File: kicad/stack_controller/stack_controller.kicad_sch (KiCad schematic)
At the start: 47 parts

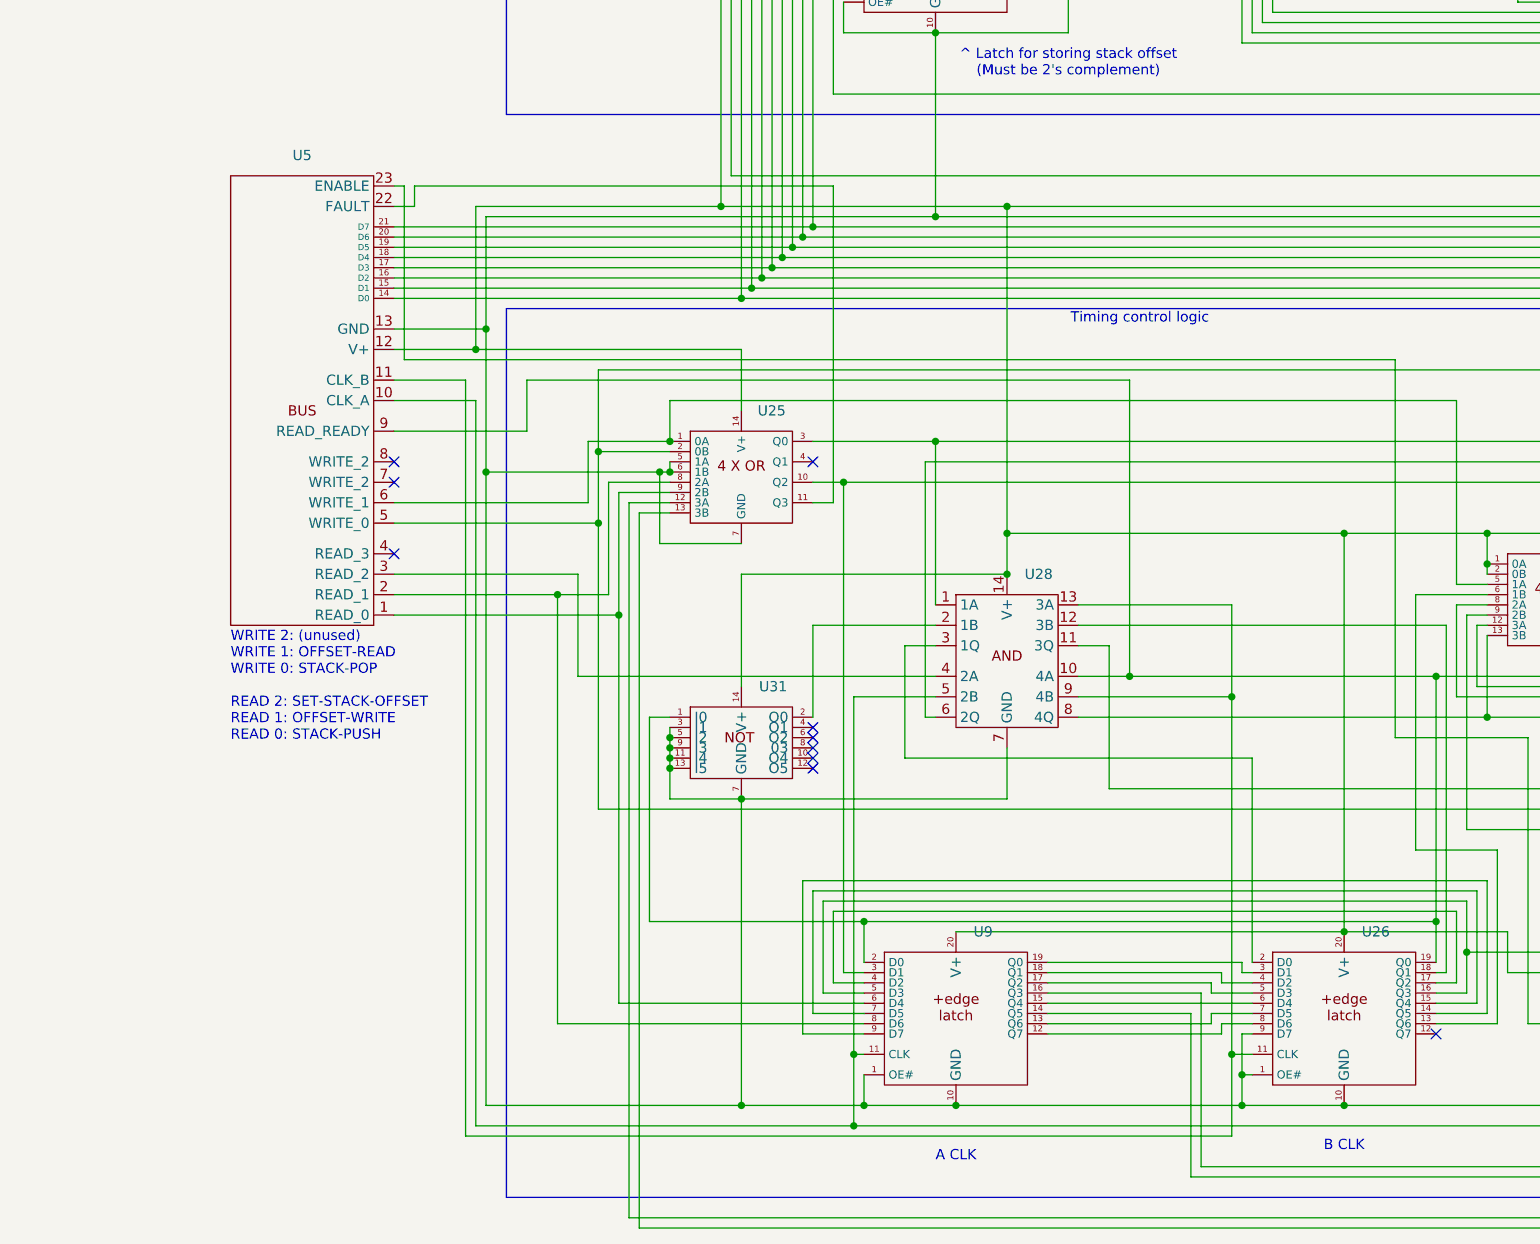
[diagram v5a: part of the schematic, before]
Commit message: Increased clock PCB clearances
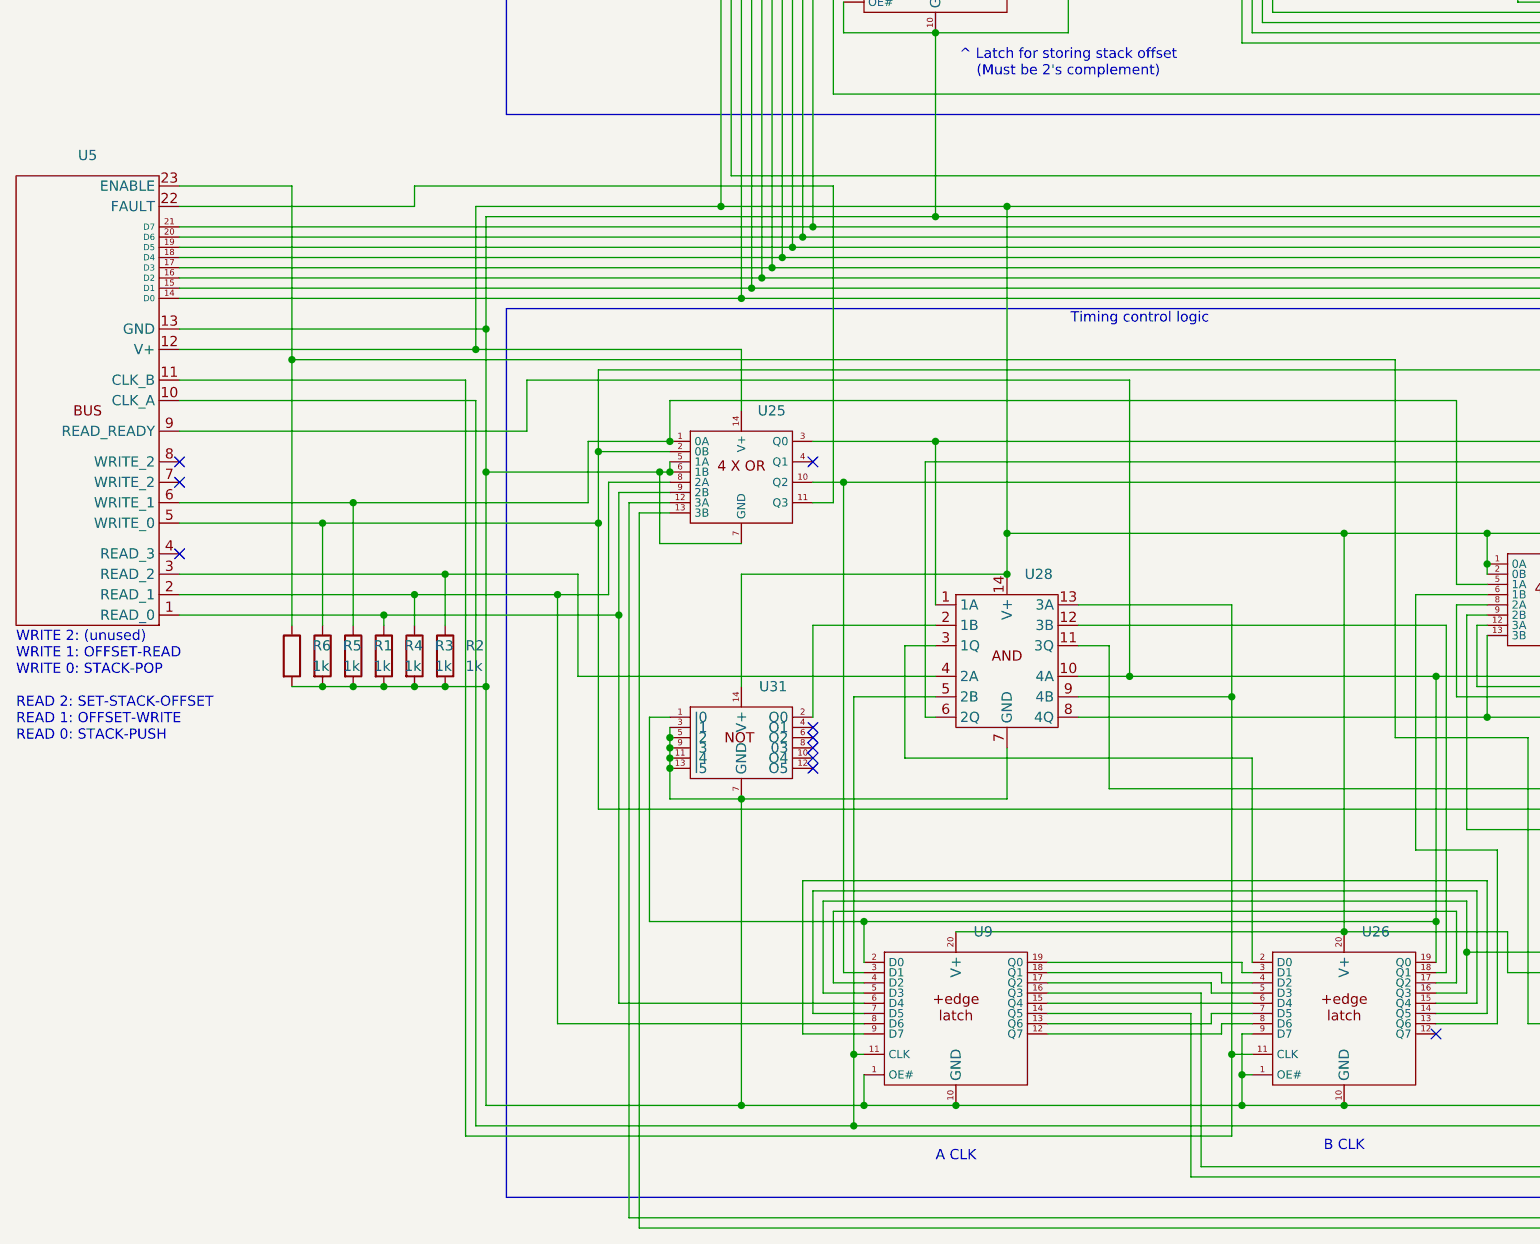
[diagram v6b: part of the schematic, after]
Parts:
- added R1, R2, R3, R4, R5, R6: 1k, custom_footprint_library:0.4_pitch_resistor, symbol Device:R
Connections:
- net at U1.7 (C_IN), U1.8 (GND), U10.14 (GND)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: now also R1.2, R2.2, R3.2, R4.2, R5.2, R6.2
- net at U25.1 (0A), U27.5 (1A), U5.6 (WRITE_1): now also R1.1
- net at U24.2 (1B), U25.2 (0B), U35.1 (IN)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: now also R5.1
- net at U25.8 (2A), U5.2 (READ_1), U9.8 (D6): now also R3.1
- net at U25.9 (2B), U5.1 (READ_0), U9.6 (D4): now also R4.1
- net at U47.2 (1B), U5.23 (ENABLE): now also R6.1
- net at U28.4 (2A), U5.3 (READ_2): now also R2.1
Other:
- moved on the sheet: U5

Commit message: Finished IO controller schematic
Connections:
- net at R1.2, R2.2, R3.2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: no longer U14.7 (C_IN)
- net at U1.16 (V+), U1.6 (B0), U10.28 (V+)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: now also U14.7 (C_IN)
- net at R6.1, U47.2 (1B): no longer U5.23 (ENABLE)
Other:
- moved on the sheet: U5
